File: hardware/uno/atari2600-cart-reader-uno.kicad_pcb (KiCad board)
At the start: 2 copper layers, 68.6 x 53.3 mm, 8 parts, among them J1 Atari 2600 Cartridge-Slot, U1 MCP23017-E/SP

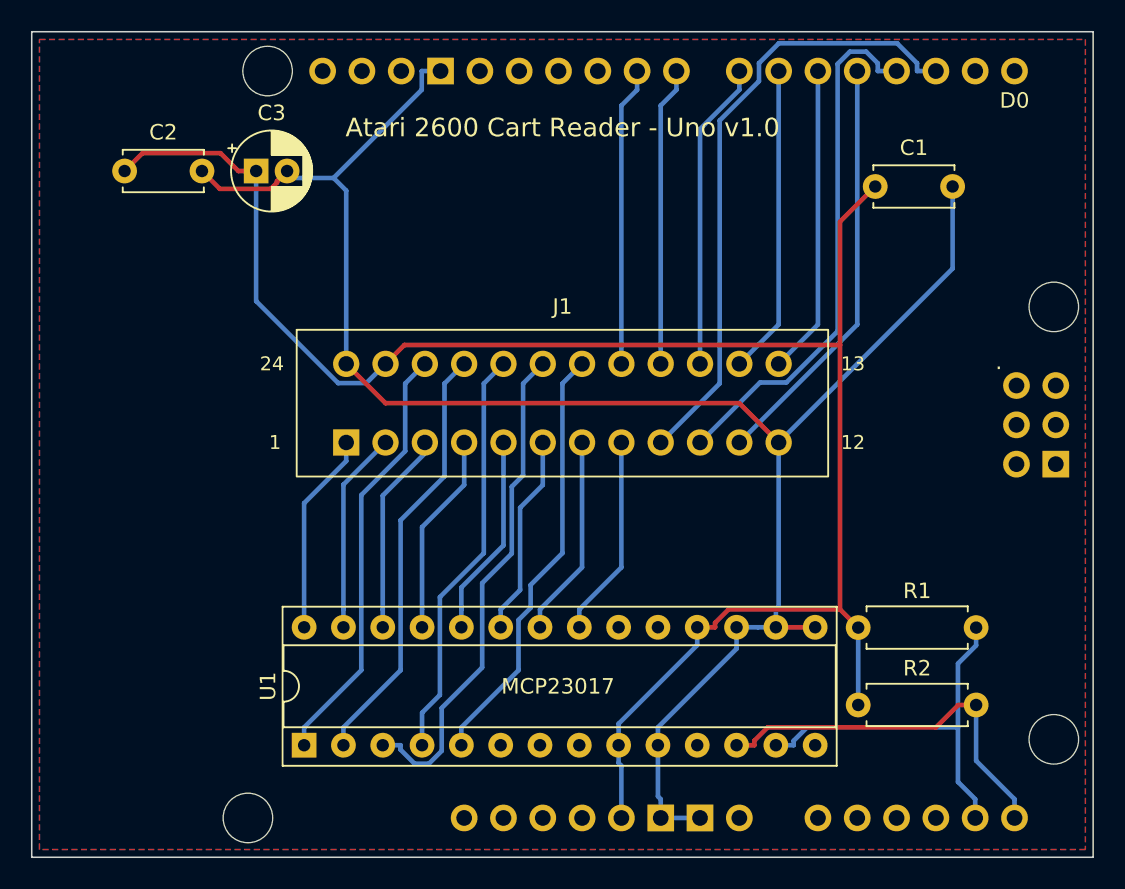
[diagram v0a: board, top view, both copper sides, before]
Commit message: Set cartridge slot row spacing to measured 5.5 mm
Stefan measured 6 mm across the outer pin edges with 0.5 mm pins.
Both shields re-routed; DRC 0 errors, 0 unconnected.

Co-Authored-By: Claude Opus 5.5 (1M context) <noreply@anthropic.com>
Claude-Session: https://claude.ai/code/session_015VQCpzuZ22TPQEmx9cLrbH
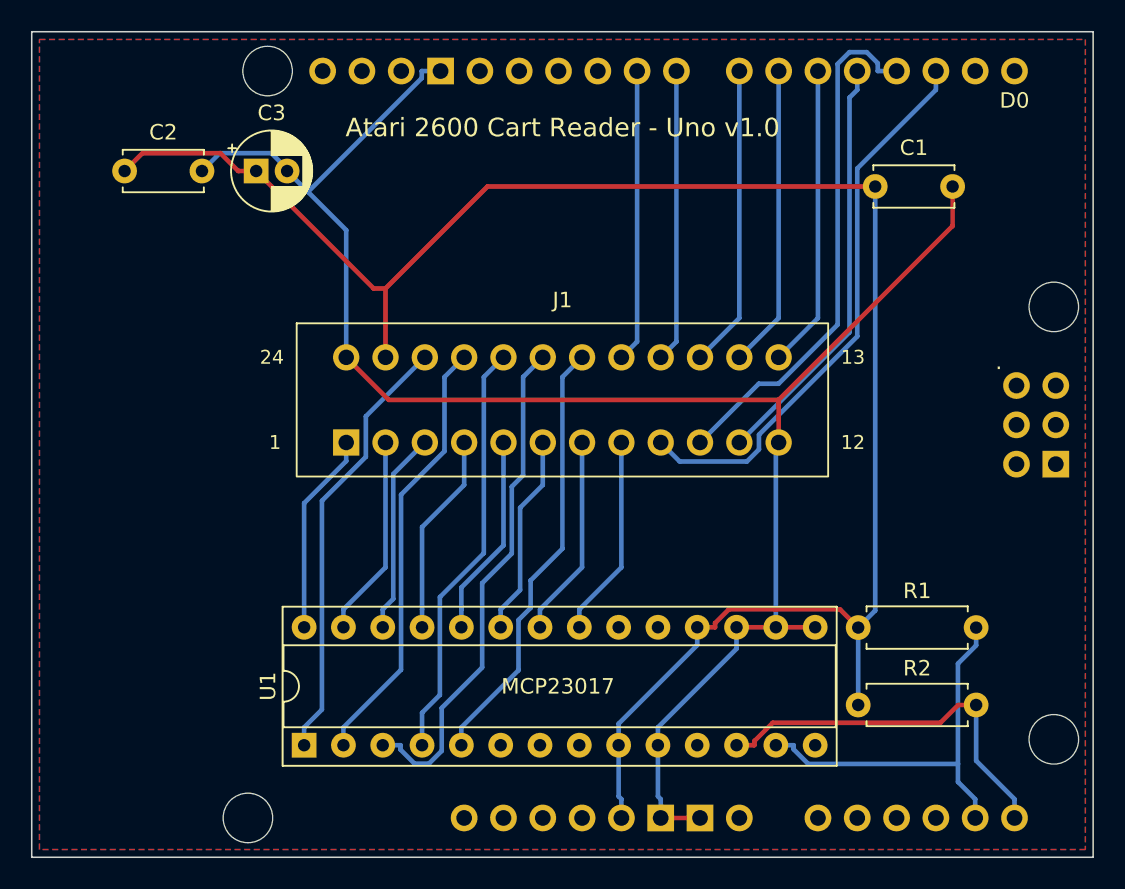
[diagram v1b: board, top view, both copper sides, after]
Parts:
- J1: footprint atari:Atari2600_Cart_Slot_2x12_P2.54mm_Row5.08mm -> atari:Atari2600_Cart_Slot_2x12_P2.54mm_Row5.50mm
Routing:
- net /D0: track 40.1 -> 36.4 mm
- net +5V: track 118.1 -> 119.8 mm
- net GND: track 117.9 -> 116.6 mm

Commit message: Switched cartridge supply, Nano board, guide mounting holes
- BC327 high-side switch with 200 mA polyfuse and rail sense on all boards
- Firmware powers the cartridge only after an orientation check
  (experimental thresholds, S command for calibration)
- New carrier board for a plugged-in Arduino Nano (same circuit and
  firmware as the Uno)
- Slot footprint with M2.5 flange holes and the guide base plate outline;
  build checks that the plate area stays free
- ICSP header removed from the shields, Uno hole next to it removed,
  Mega slot moved to the board centre
- Fix: struct Scheme declared before Arduino's generated prototypes
  (the sketch did not compile before)
- Switch schematic and prototype photos

Co-Authored-By: Claude Opus 5.5 (1M context) <noreply@anthropic.com>
Claude-Session: https://claude.ai/code/session_015VQCpzuZ22TPQEmx9cLrbH
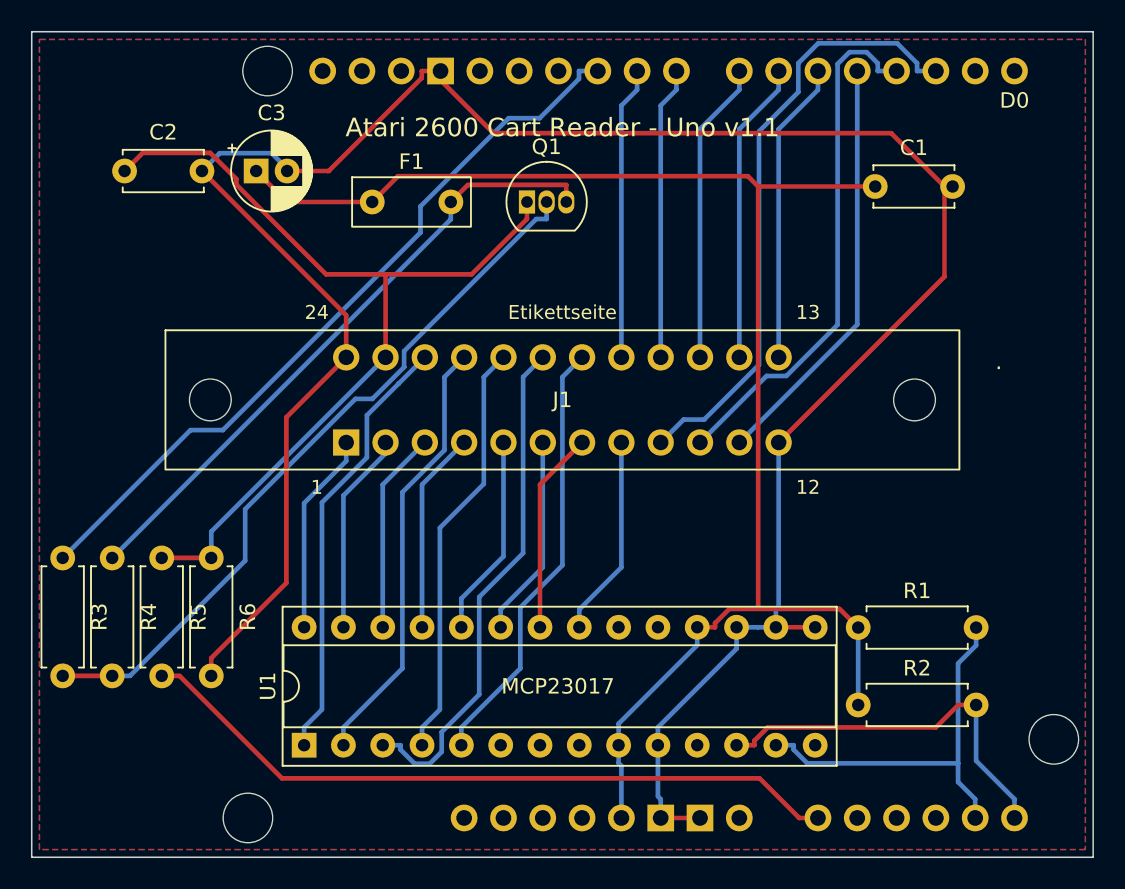
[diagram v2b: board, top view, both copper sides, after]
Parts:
- added F1: MF-R020 (200 mA), atari:Fuse_PTC_Radial_P5.08mm, F.Cu at (122.0, 111.0)
- added Q1: BC327, Package_TO_SOT_THT:TO-92_Inline, F.Cu at (132.0, 111.0)
- added R3: 1k, Resistor_THT:R_Axial_DIN0207_L6.3mm_D2.5mm_P7.62mm_Horizontal, F.Cu at (102.0, 134.0)
- added R4: 10k, Resistor_THT:R_Axial_DIN0207_L6.3mm_D2.5mm_P7.62mm_Horizontal, F.Cu at (105.2, 134.0)
- added R5: 10k, Resistor_THT:R_Axial_DIN0207_L6.3mm_D2.5mm_P7.62mm_Horizontal, F.Cu at (108.4, 134.0)
- added R6: 100k, Resistor_THT:R_Axial_DIN0207_L6.3mm_D2.5mm_P7.62mm_Horizontal, F.Cu at (111.6, 134.0)
- J1: footprint atari:Atari2600_Cart_Slot_2x12_P2.54mm_Row5.50mm -> atari:Atari2600_Cart_Slot_2x12_P2.54mm_Row5.50mm_Guide
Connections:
- A1 pad A0: (no net) -> /CART_SENSE
- A1 pad D10: (no net) -> /CART_PWR
- C2 pad 1: +5V -> /CART_5V
- J1 pad 23: +5V -> /CART_5V
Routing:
- net /CART_5V: track 0.00 -> 58.7 mm
- net /CART_PWR: track 0.00 -> 48.9 mm
- net /Q_BASE: track 0.00 -> 47.2 mm
- net /CART_SENSE: track 0.00 -> 46.2 mm
- net /+5V_F: track 0.00 -> 41.1 mm
- net GND: track 116.6 -> 151.4 mm
- net +5V: track 119.8 -> 100.1 mm
- net /D0: track 36.4 -> 39.4 mm
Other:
- board text added: "Atari 2600 Cart Reader - Uno v1.1"
- board text removed: "Atari 2600 Cart Reader - Uno v1.0"

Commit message: Silkscreen: reference and value per part, fambach.net on the front
labels.py adds the silkscreen texts after routing, so the copper stays unchanged.

Co-Authored-By: Claude Opus 5.5 <noreply@anthropic.com>
Claude-Session: https://claude.ai/code/session_015VQCpzuZ22TPQEmx9cLrbH
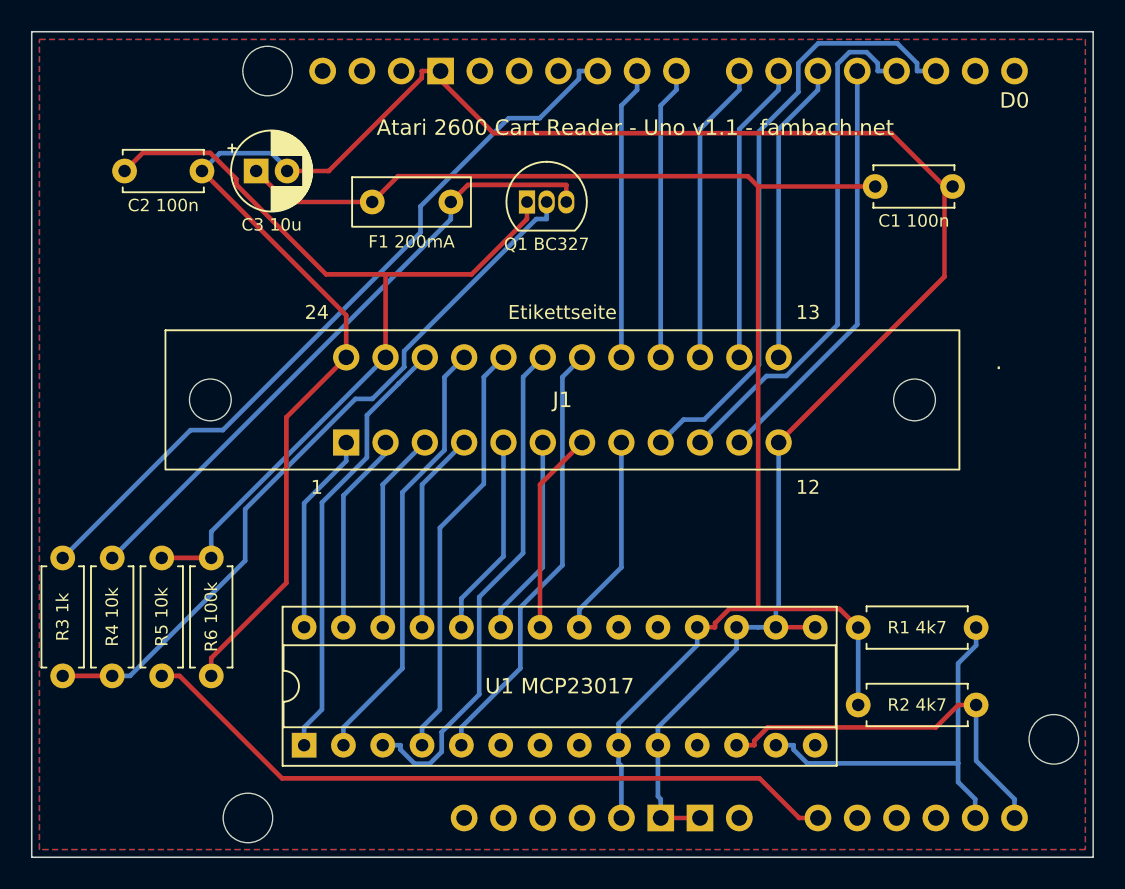
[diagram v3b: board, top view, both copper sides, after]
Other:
- board text added: "Atari 2600 Cart Reader - Uno v1.1 - fambach.net"
- board text added: "C1 100n"
- board text added: "C2 100n"
- board text added: "C3 10u"
- board text added: "F1 200mA"
- board text added: "Q1 BC327"
- board text added: "R1 4k7"
- board text added: "R2 4k7"
- board text added: "R3 1k"
- board text added: "R4 10k"
- board text added: "R5 10k"
- board text added: "R6 100k"
- board text added: "U1 MCP23017"
- board text removed: "Atari 2600 Cart Reader - Uno v1.1"
- board text removed: "MCP23017"
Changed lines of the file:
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@@
     (tags "Resistor Axial_DIN0207 series Axial Horizontal pin pitch 7.62mm 0.25W = 1/4W length 6.3mm diameter 2.5mm")
     (attr through_hole)
-    (fp_text reference "R1" (at 3.81 -2.37) (layer "F.SilkS")
+    (fp_text reference "R1" (at 3.81 -2.37) (layer "F.SilkS") hide
         (effects (font (size 1 1) (thickness 0.15)))
     )
@@
     (tags "C Disc series Radial pin pitch 5.00mm  diameter 5mm width 2.5mm Capacitor")
     (attr through_hole)
-    (fp_text reference "C1" (at 2.5 -2.5) (layer "F.SilkS")
+    (fp_text reference "C1" (at 2.5 -2.5) (layer "F.SilkS") hide
         (effects (font (size 1 1) (thickness 0.15)))
     )
@@
     (tags "Resistor Axial_DIN0207 series Axial Horizontal pin pitch 7.62mm 0.25W = 1/4W length 6.3mm diameter 2.5mm")
     (attr through_hole)
-    (fp_text reference "R4" (at 3.81 -2.37 -90) (layer "F.SilkS")
+    (fp_text reference "R4" (at 3.81 -2.37 -90) (layer "F.SilkS") hide
         (effects (font (size 1 1) (thickness 0.15)))
     )
@@
     (tags "Resistor Axial_DIN0207 series Axial Horizontal pin pitch 7.62mm 0.25W = 1/4W length 6.3mm diameter 2.5mm")
     (attr through_hole)
-    (fp_text reference "R3" (at 3.81 -2.37 -90) (layer "F.SilkS")
+    (fp_text reference "R3" (at 3.81 -2.37 -90) (layer "F.SilkS") hide
         (effects (font (size 1 1) (thickness 0.15)))
     )
@@
     (tags "to-92 sc-43 sc-43a sot54 PA33 transistor")
     (attr through_hole)
-    (fp_text reference "Q1" (at 1.27 -3.56) (layer "F.SilkS")
+    (fp_text reference "Q1" (at 1.27 -3.56) (layer "F.SilkS") hide
         (effects (font (size 1 1) (thickness 0.15)))
     )
@@
     (tags "Resistor Axial_DIN0207 series Axial Horizontal pin pitch 7.62mm 0.25W = 1/4W length 6.3mm diameter 2.5mm")
     (attr through_hole)
-    (fp_text reference "R2" (at 3.81 -2.37) (layer "F.SilkS")
+    (fp_text reference "R2" (at 3.81 -2.37) (layer "F.SilkS") hide
         (effects (font (size 1 1) (thickness 0.15)))
     )
@@
     (tags "CP Radial series Radial pin pitch 2.00mm  diameter 5mm Electrolytic Capacitor")
     (attr through_hole)
-    (fp_text reference "C3" (at 1 -3.75) (layer "F.SilkS")
+    (fp_text reference "C3" (at 1 -3.75) (layer "F.SilkS") hide
         (effects (font (size 1 1) (thickness 0.15)))
     )
@@
     (tags "Resistor Axial_DIN0207 series Axial Horizontal pin pitch 7.62mm 0.25W = 1/4W length 6.3mm diameter 2.5mm")
     (attr through_hole)
-    (fp_text reference "R5" (at 3.81 -2.37 -90) (layer "F.SilkS")
+    (fp_text reference "R5" (at 3.81 -2.37 -90) (layer "F.SilkS") hide
         (effects (font (size 1 1) (thickness 0.15)))
     )
@@
     (tags "Resistor Axial_DIN0207 series Axial Horizontal pin pitch 7.62mm 0.25W = 1/4W length 6.3mm diameter 2.5mm")
     (attr through_hole)
-    (fp_text reference "R6" (at 3.81 -2.37 -90) (layer "F.SilkS")
+    (fp_text reference "R6" (at 3.81 -2.37 -90) (layer "F.SilkS") hide
         (effects (font (size 1 1) (thickness 0.15)))
     )
@@
     (tags "THT DIP DIL PDIP 2.54mm 7.62mm 300mil Socket")
     (attr through_hole)
-    (fp_text reference "U1" (at 3.81 -2.33 90) (layer "F.SilkS")
+    (fp_text reference "U1" (at 3.81 -2.33 90) (layer "F.SilkS") hide
         (effects (font (size 1 1) (thickness 0.15)))
     )
@@
     (tags "C Disc series Radial pin pitch 5.00mm  diameter 5mm width 2.5mm Capacitor")
     (attr through_hole)
-    (fp_text reference "C2" (at 2.5 -2.5) (layer "F.SilkS")
+    (fp_text reference "C2" (at 2.5 -2.5) (layer "F.SilkS") hide
         (effects (font (size 1 1) (thickness 0.15)))
     )
@@
     (tags "polyfuse PTC radial")
     (attr through_hole)
-    (fp_text reference "F1" (at 2.54 -2.6) (layer "F.SilkS")
+    (fp_text reference "F1" (at 2.54 -2.6) (layer "F.SilkS") hide
         (effects (font (size 1 1) (thickness 0.15)))
     )
@@
   (gr_line (start 100 153.34) (end 100 100)
     (stroke (width 0.1) (type default)) (layer "Edge.Cuts"))
+  (gr_text "github.com/sfambach/arduino-atari2600-cart-reader" (at 134.3 115.5) (layer "B.SilkS")
+    (effects (font (size 0.8 0.8) (thickness 0.12)) (justify mirror))
+  )
   (gr_text "fambach.net" (at 134.3 113.5) (layer "B.SilkS")
     (effects (font (size 1 1) (thickness 0.15)) (justify mirror))
   )
-  (gr_text "github.com/sfambach/arduino-atari2600-cart-reader" (at 134.3 115.5) (layer "B.SilkS")
-    (effects (font (size 0.8 0.8) (thickness 0.12)) (justify mirror))
-  )
-  (gr_text "Atari 2600 Cart Reader - Uno v1.1" (at 134.3 106.2) (layer "F.SilkS")
-    (effects (font (size 1.2 1.2) (thickness 0.18)))
-  )
-  (gr_text "MCP23017" (at 134 142.3) (layer "F.SilkS")
+  (gr_text "R3 1k" (at 102 137.81 90) (layer "F.SilkS")
+    (effects (font (size 0.8 0.8) (thickness 0.12)))
+  )
+  (gr_text "Q1 BC327" (at 133.27 113.735) (layer "F.SilkS")
+    (effects (font (size 0.8 0.8) (thickness 0.12)))
+  )
+  (gr_text "Atari 2600 Cart Reader - Uno v1.1 - fambach.net" (at 139 106.2) (layer "F.SilkS")
     (effects (font (size 1 1) (thickness 0.15)))
   )
+  (gr_text "C2 100n" (at 108.5 111.225) (layer "F.SilkS")
+    (effects (font (size 0.8 0.8) (thickness 0.12)))
+  )
+  (gr_text "R5 10k" (at 108.4 137.81 90) (layer "F.SilkS")
+    (effects (font (size 0.8 0.8) (thickness 0.12)))
+  )
+  (gr_text "F1 200mA" (at 124.54 113.575) (layer "F.SilkS")
+    (effects (font (size 0.8 0.8) (thickness 0.12)))
+  )
+  (gr_text "R6 100k" (at 111.599999 137.81 90) (layer "F.SilkS")
+    (effects (font (size 0.8 0.8) (thickness 0.12)))
+  )
+  (gr_text "R2 4k7" (at 157.21 143.5) (layer "F.SilkS")
+    (effects (font (size 0.8 0.8) (thickness 0.12)))
+  )
+  (gr_text "U1 MCP23017" (at 134.109999 142.289999) (layer "F.SilkS")
+    (effects (font (size 1 1) (thickness 0.15)))
+  )
+  (gr_text "R1 4k7" (at 157.21 138.5) (layer "F.SilkS")
+    (effects (font (size 0.8 0.8) (thickness 0.12)))
+  )
+  (gr_text "R4 10k" (at 105.2 137.81 90) (layer "F.SilkS")
+    (effects (font (size 0.8 0.8) (thickness 0.12)))
+  )
+  (gr_text "C1 100n" (at 157 112.225) (layer "F.SilkS")
+    (effects (font (size 0.8 0.8) (thickness 0.12)))
+  )
+  (gr_text "C3 10u" (at 115.5 112.475) (layer "F.SilkS")
+    (effects (font (size 0.8 0.8) (thickness 0.12)))
+  )
   (segment (start 144.1519 138.2114) (end 144.1519 138.48) (width 0.3) (layer "F.Cu") (net 1))

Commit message: Reset and read buttons on all boards (v1.2)
SW1 resets the Arduino, SW2 on A1 repeats the last dump; dump.py listen saves button dumps.

Co-Authored-By: Claude Opus 5.5 <noreply@anthropic.com>
Claude-Session: https://claude.ai/code/session_015VQCpzuZ22TPQEmx9cLrbH
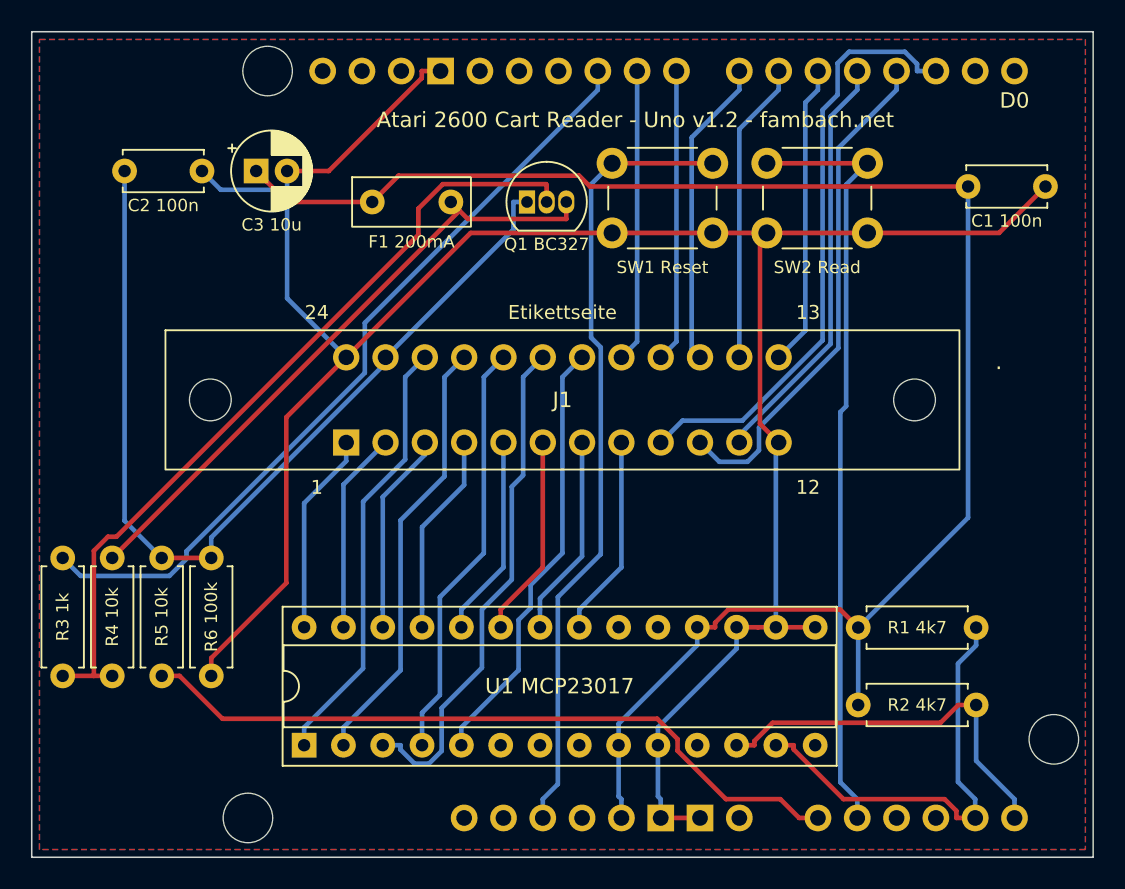
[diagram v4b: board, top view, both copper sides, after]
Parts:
- added SW1: Reset, Button_Switch_THT:SW_PUSH_6mm, F.Cu at (137.5, 108.5)
- added SW2: Read, Button_Switch_THT:SW_PUSH_6mm, F.Cu at (147.5, 108.5)
- moved C1 6.00 mm to (160.5, 110.0)
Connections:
- A1 pad A1: (no net) -> /READ
- A1 pad RST1: (no net) -> /RESET
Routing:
- net /RESET: track 0.00 -> 51.2 mm
- net /READ: track 0.00 -> 50.0 mm
- net +5V: track 100.1 -> 110.3 mm
- net /Q_BASE: track 47.2 -> 52.5 mm
- net GND: track 151.4 -> 154.8 mm
- net /SDA: track 25.7 -> 28.5 mm
- net /CART_PWR: track 48.9 -> 51.5 mm
- net /CART_5V: track 58.7 -> 61.2 mm
- net /D1: track 33.8 -> 32.8 mm
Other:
- board text added: "Atari 2600 Cart Reader - Uno v1.2 - fambach.net"
- board text added: "SW1 Reset"
- board text added: "SW2 Read"
- board text removed: "Atari 2600 Cart Reader - Uno v1.1 - fambach.net"
